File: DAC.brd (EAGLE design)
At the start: 160 x 100 mm, 119 parts, among them IC1 XHRA-2HPA, IC10 TLE2141ACP, IC2 STF202-22T1G, IC3 ADM1085AKSZ-REEL7, IC4 STM1061N38WX6F, IC5 SN74LVC1G06, IC6 PCM1795DB, IC7 LME49720NA_NOPB, IC8 LME49720NA_NOPB, IC9 LME49720NA_NOPB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

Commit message: Add layout progress
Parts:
- removed C16, C17, C18: 100n, resistor:C0603K
- removed C26, C28, C29, C32: 10u, resistor:A/3216-18R
- removed JP10, JP12, JP13, JP14, JP15, JP16, JP17, JP18, JP19, JP5, JP6, JP7, JP8, JP9: (no value), pinhead:1X01
- removed JP2, JP3: (no value), pinhead:1X08
- added GND, GPI: (no value), pinhead:1X03
- added J10, J12, J13, J14, J15, J16, J17, J18, J19, J5, J6, J7, J8, J9: (no value), pinhead:1X01
- moved R33 112.4 mm to (10.5, 16.4)
- moved R3 107.3 mm to (22.7, 64.8), turned to 270 degrees
- moved C24 104.0 mm to (24.6, 33.0), turned to 270 degrees
- moved R37 103.9 mm to (5.71, 16.4), turned to 180 degrees
- moved R35 100.6 mm to (5.71, 20.7), turned to 180 degrees
- moved R7 100.3 mm to (16.3, 49.5), turned to 180 degrees
- moved C30 100.1 mm to (6.60, 13.1), turned to 180 degrees
- moved C27 99.9 mm to (30.2, 33.0), turned to 270 degrees
- moved C43 98.0 mm to (5.71, 18.5), turned to 180 degrees
- moved R32 97.9 mm to (17.0, 30.2), turned to 90 degrees
- moved R36 97.5 mm to (21.0, 26.5)
- moved R8 95.9 mm to (16.3, 47.4), turned to 180 degrees
- moved C41 95.9 mm to (17.5, 25.4), turned to 270 degrees
- moved C44 95.6 mm to (10.2, 13.1), turned to 0 degrees
- moved IC10 95.2 mm to (10.5, 7.49), turned to 90 degrees
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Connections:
- net 1V: now also J7.1; no longer C16.1, C17.1, C18.1, JP7.1
- net 3.3V: now also J6.1; no longer C26.+, JP6.1
- net 5V: now also J5.1; no longer C28.+, C29.+, C32.+, JP3.1, JP3.2, JP3.3, JP3.4, JP5.1
- net D0: now also J14.1; no longer JP14.1
- net D1: now also J15.1; no longer JP15.1
- net D2: now also J16.1; no longer JP16.1
- net D3: now also J17.1; no longer JP17.1
- net DAC_RST: now also J18.1; no longer JP18.1
- net GND: now also GND.1, GND.2, GND.3; no longer C16.2, C17.2, C18.2, C26.-, C28.-, C29.-, C32.-, JP3.5, JP3.6, JP3.7, JP3.8
- net GPI_0: no longer JP2.1
- net GPI_1: no longer JP2.2
- net GPI_2: no longer JP2.7
- net GPI_3: now also GPI.1; no longer JP2.4
- net GPI_4: now also GPI.2; no longer JP2.5
- net GPI_5: now also GPI.3; no longer JP2.6
- net GPI_6: no longer JP2.3
- net GPI_7: no longer JP2.8
- net MCLK: now also J8.1; no longer JP8.1
- net MCLK_SEL: now also J9.1; no longer JP9.1
- net N_MCLK_SEL: now also J10.1; no longer JP10.1
- net SPI_CLK: now also J13.1; no longer JP13.1
- net SPI_CS: now also J12.1; no longer JP12.1
- net VGND: now also J19.1; no longer JP19.1
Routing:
- net VGND: track 0.00 -> 92.6 mm
- net 1V: track 2.68 -> 60.0 mm, vias 0 -> 5
- net IL+: track 0.00 -> 50.0 mm
- net IR+: track 0.00 -> 31.6 mm
- net AUDIO_LEFT: track 0.00 -> 31.1 mm
- net MCLK: track 0.00 -> 29.5 mm
- net AUDIO_RIGHT: track 0.00 -> 29.0 mm
- net IL-: track 0.00 -> 28.9 mm
- net SPI_CS: track 1.16 -> 29.8 mm, vias 1 -> 0
- net D0: track 0.00 -> 27.8 mm
- net MCLK_SEL: track 0.00 -> 26.9 mm, vias 0 -> 1
- net N$46: track 0.00 -> 24.7 mm
- net BCK: track 0.00 -> 24.4 mm
- net RST_N: track 0.00 -> 24.2 mm, vias 0 -> 2
- net DATA: track 0.00 -> 24.0 mm
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- added copper zone on layer 1, net GND
- removed copper zone on layer 1, net 3.3V
- removed copper zone on layer 16, net 5V
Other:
- board size 160 x 100 mm -> 54.8 x 79.7 mm

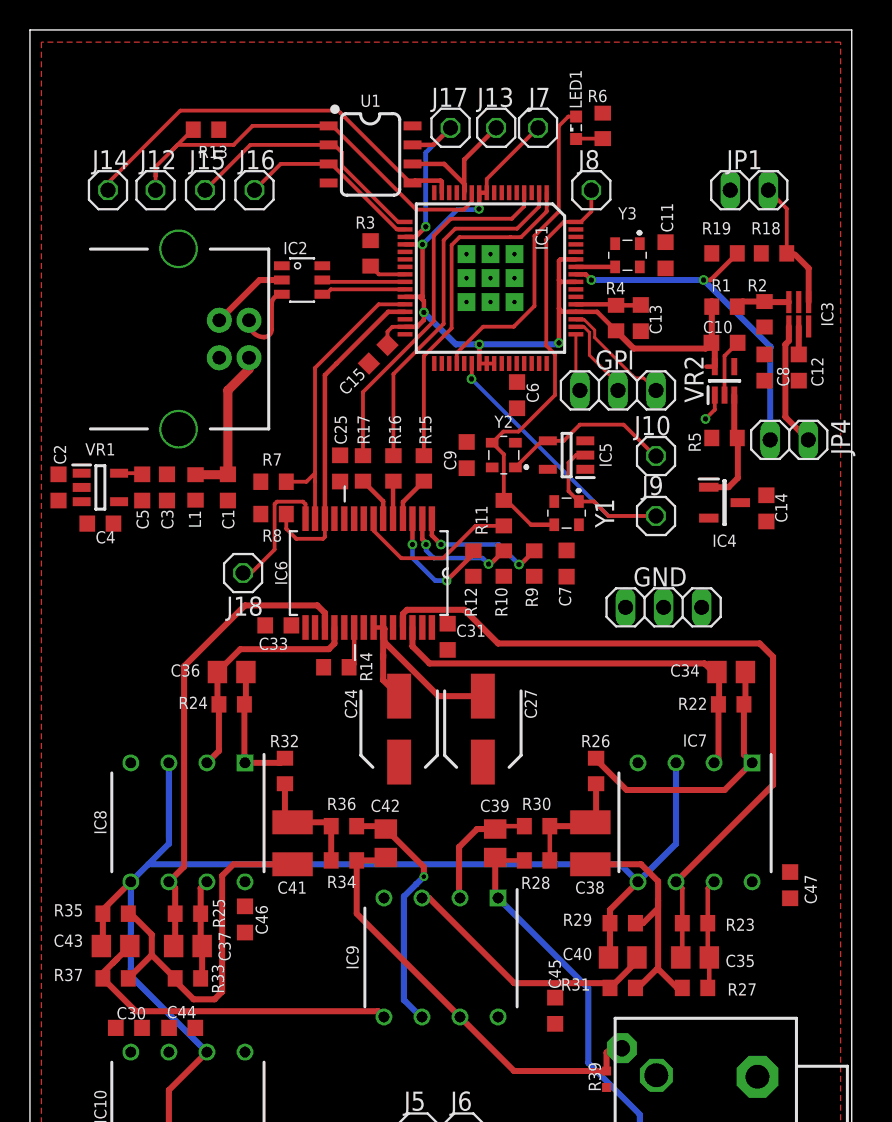
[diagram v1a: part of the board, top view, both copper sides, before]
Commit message: Add more layout progress
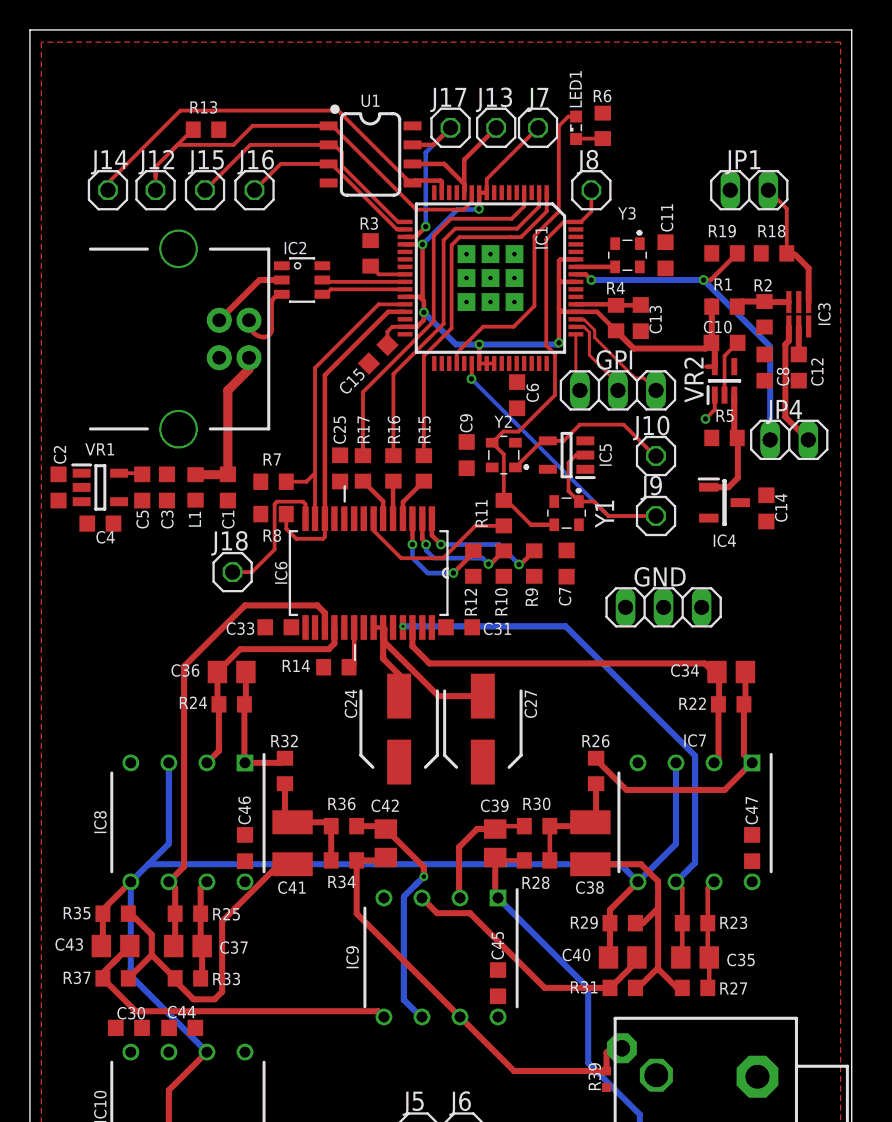
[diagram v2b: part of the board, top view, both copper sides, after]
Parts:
- moved C46 4.76 mm to (14.4, 25.1), turned to 90 degrees
- moved C45 4.23 mm to (31.2, 16.1)
- moved C47 3.55 mm to (48.2, 25.1)
- moved C31 0.99 mm to (28.6, 39.8), turned to 0 degrees
- moved J18 0.70 mm to (13.5, 43.5)
- moved C33 0.13 mm to (16.6, 39.8)
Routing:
- net IL+: track 50.0 -> 37.4 mm, vias 0 -> 1
- net N$46: track 24.7 -> 22.9 mm
- net DAC_RST: track 8.95 -> 9.62 mm
